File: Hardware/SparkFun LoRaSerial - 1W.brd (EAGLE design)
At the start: 50.8 x 27.9 mm, 73 parts, among them J1 QWIIC_RIGHT_ANGLE, J3 USB C, J4 JTAG, U2 ATSAMD21G-A, U3 AP2112K-3.3, U4 E19-915M30S, Y1 32.768kHz

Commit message: File rename
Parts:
- removed U$8: (no value), output:LORA_1W0
- added S1: Reset, SparkFun-Switches:TACTILE_SWITCH_SMD_RIGHT_ANGLE
- added U$18: (no value), output:LORASERIAL0
- U$1: device output:SERIAL0 -> output:1W1
- U$4: device output:TELEMETRY1 -> output:TRAIN0
- moved LOGO5 21.9 mm to (39.6, 23.2)
- moved U$4 15.6 mm to (45.7, 12.7), turned to 90 degrees
- moved LOGO3 3.84 mm to (43.6, 5.08), turned to 90 degrees
- moved U$5 3.81 mm to (37.0, 25.4)
- moved J1 3.81 mm to (46.0, 5.08)
- moved U$1 1.53 mm to (33.0, 25.4)
- moved JP9 1.27 mm to (39.4, 7.62)
- moved R3 1.27 mm to (41.9, 10.2)
- moved R6 1.27 mm to (41.9, 5.08)
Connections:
- net BOARD_ID renamed A2/BOARD_ID
- net SPI_PICO renamed D11/SPI_PICO
- net SPI_POCI renamed D12/SPI_POCI
- net SPI_SCK renamed D13/SPI_SCK
- removed net A3: U2.9
- new net A3/TRAIN: S1.2, U2.9
- new net A4: U2.10
- new net A5: U2.47
- new net D30: U2.37
- new net D31: U2.38
- net GND: now also S1.1
- net RX_LED: no longer U2.48
- net TX_LED: no longer U2.39
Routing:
- net SDA: track 38.9 -> 29.1 mm
- net SDA_PU1: track 2.81 -> 0.00 mm
- net 3.3V: track 91.9 -> 93.5 mm
- net SCL: track 39.7 -> 41.0 mm
- net RX_LED: track 29.5 -> 28.4 mm
- net TX_LED: track 18.5 -> 17.6 mm
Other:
- outline, holes or cut-outs redrawn

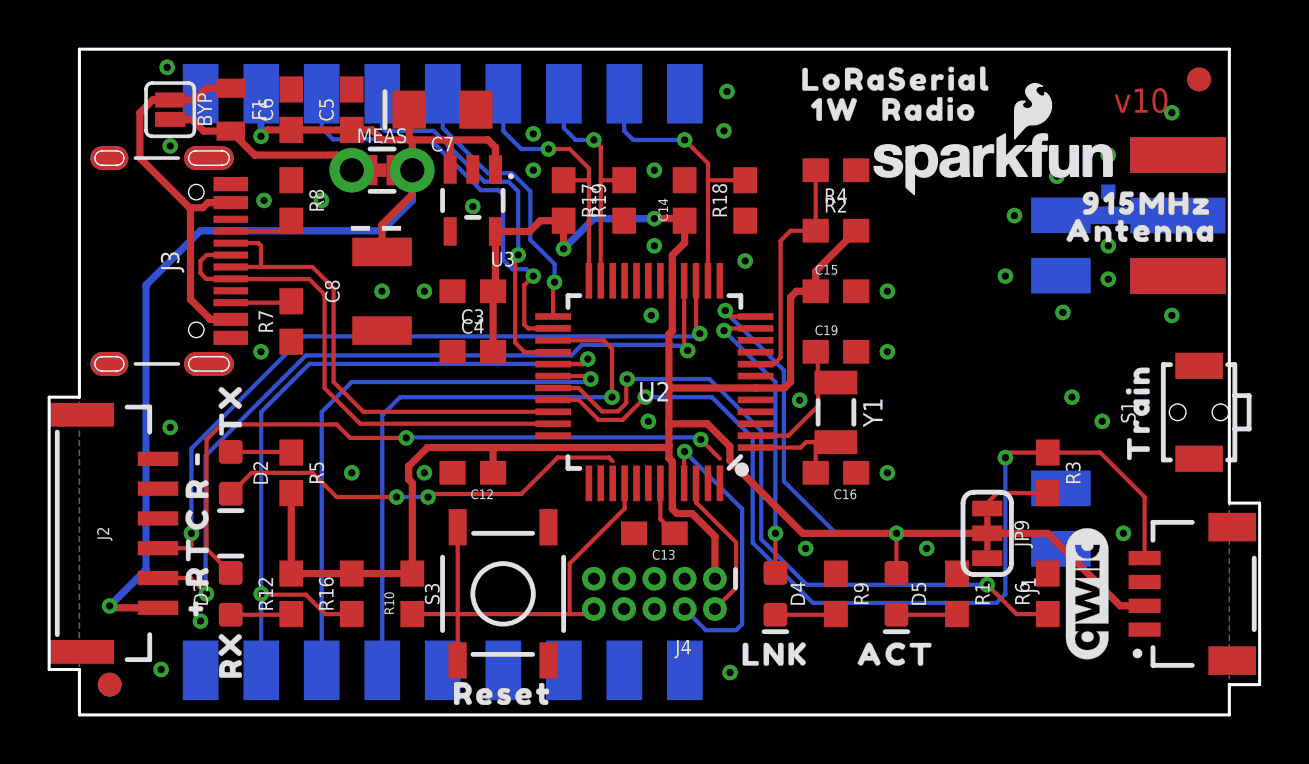
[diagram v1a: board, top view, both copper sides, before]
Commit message: Add train button, TX/RX LEDs, CTS/RTS connections, GPIO breakout. Increase to v11.
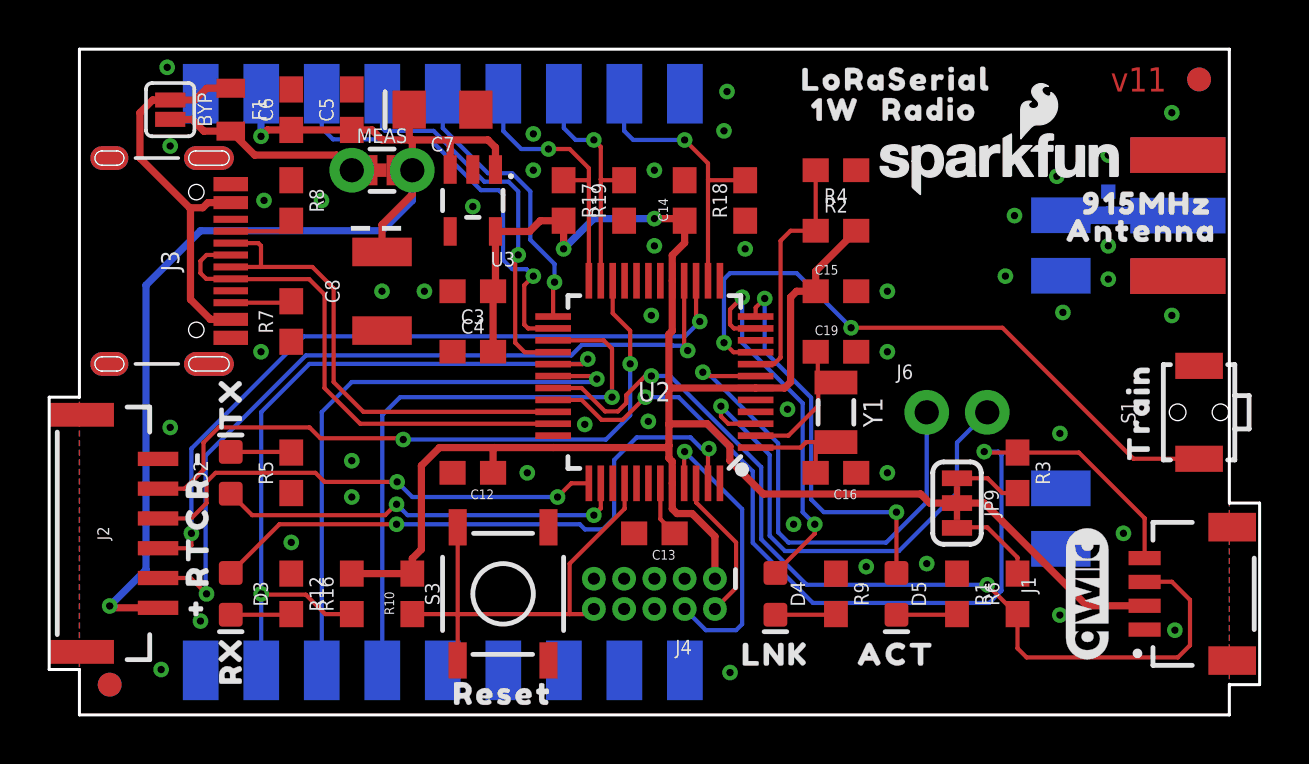
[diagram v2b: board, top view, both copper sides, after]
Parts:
- added J6: (no value), SparkFun-Connectors:1X02_NO_SILK
- D6: value PESD0402-0402T -> PESD0402
- S1: value Reset -> Train
- moved JP9 1.80 mm to (38.1, 8.89)
- moved R3 1.27 mm to (40.6, 10.2)
- moved R6 1.27 mm to (40.6, 5.08)
- moved U$10 0.25 mm to (7.62, 2.29)
- moved U$11 0.25 mm to (7.62, 13.1)
- moved LOGO5 0.25 mm to (39.9, 23.2)
- turned D2 to 90 degrees
- turned D3 to 270 degrees
- turned R12 to 270 degrees
- turned R5 to 90 degrees
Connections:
- net AREF renamed D42/AREF
- net SCL renamed D21/SCL
- net SDA renamed D20/SDA
- net USB_D+ renamed D29/USB_D+
- net USB_D- renamed D28/USB_D-
- net USB_HOST_EN renamed D27/USB_HOST_EN
- removed net A5: U2.47
- removed net CTS-I: J2.3
- removed net D30: U2.37
- removed net D31: U2.38
- removed net LORA_D2: U4.5
- removed net N$5: D2.A, R5.1
- removed net N$9: D3.A, R12.1
- removed net RTS-O: J2.2
- removed net RX_LED: D3.C
- removed net TX_LED: D2.C
- new net A5/RX_LED: D3.A, U2.47
- new net D22: U2.21
- new net D23: U2.19
- new net D24: U2.20
- new net D30/CTS-I: J2.3, U2.37
- new net D31/TX_LED: D2.A, U2.38
- new net D38/RTS-O: J2.2, U2.22
- new net N$3: D3.C, R12.2
- new net N$4: D2.C, R5.2
- net 3.3V: no longer R12.2, R5.2
- net A0: now also J6.2
- net A1: now also J6.1
- net A3/TRAIN: now also S1.1; no longer S1.2
- net GND: now also R12.1, R5.1, S1.2; no longer S1.1
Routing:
- net RX_LED: track 28.4 -> 0.00 mm, vias 2 -> 0
- net D38/RTS-O: track 0.00 -> 28.1 mm, vias 0 -> 2
- net A3/TRAIN: track 0.00 -> 27.4 mm, vias 0 -> 2
- net A5/RX_LED: track 0.00 -> 25.7 mm, vias 0 -> 2
- net A0: track 0.00 -> 21.3 mm, vias 0 -> 1
- net A1: track 0.00 -> 21.3 mm, vias 0 -> 1
- net D30/CTS-I: track 0.00 -> 20.1 mm, vias 0 -> 2
- net TX_LED: track 17.6 -> 0.00 mm, vias 2 -> 0
- net D31/TX_LED: track 0.00 -> 17.5 mm, vias 0 -> 2
- net D20/SDA: track 29.1 -> 39.8 mm
- net 3.3V: track 93.5 -> 87.1 mm
- net SDA_PU1: track 0.00 -> 3.75 mm
- net D8/LINK: track 12.4 -> 16.0 mm
- net N$5: track 2.55 -> 0.00 mm
- net N$4: track 0.00 -> 2.55 mm
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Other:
- board text added: "v11"
- board text removed: "v10"
